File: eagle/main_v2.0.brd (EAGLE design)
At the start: 95 x 78 mm, 97 parts, among them IC1 74HC257D, IC2 PCA9530, IC3 RAC04, IC4 CS8416, IC5 MCP130-300I/SN, IC6 MAX1724, K1 G6A-234P, T1 BC847, T2 BC857, T3 BC847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

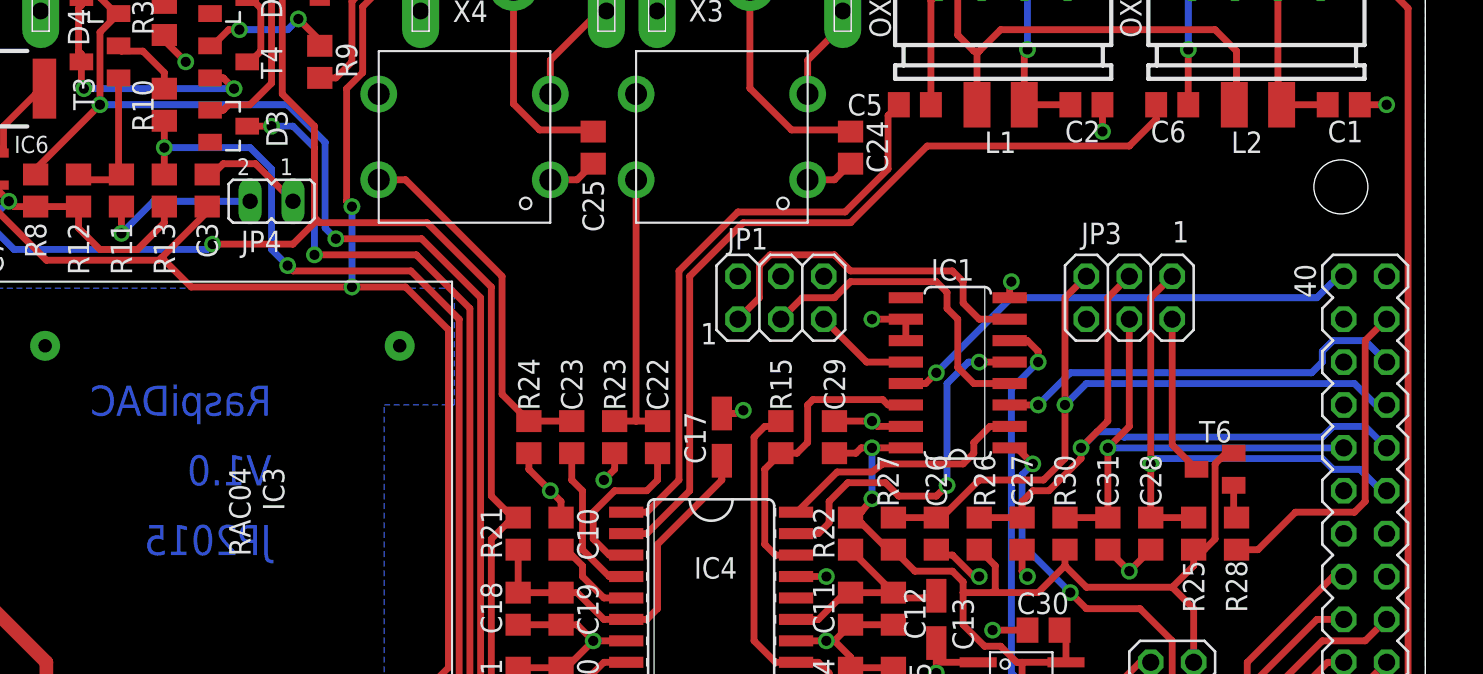
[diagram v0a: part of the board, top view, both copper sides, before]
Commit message: Eagle-Files: V2.0, zusätzlichen Ausgang für Relais eingebaut
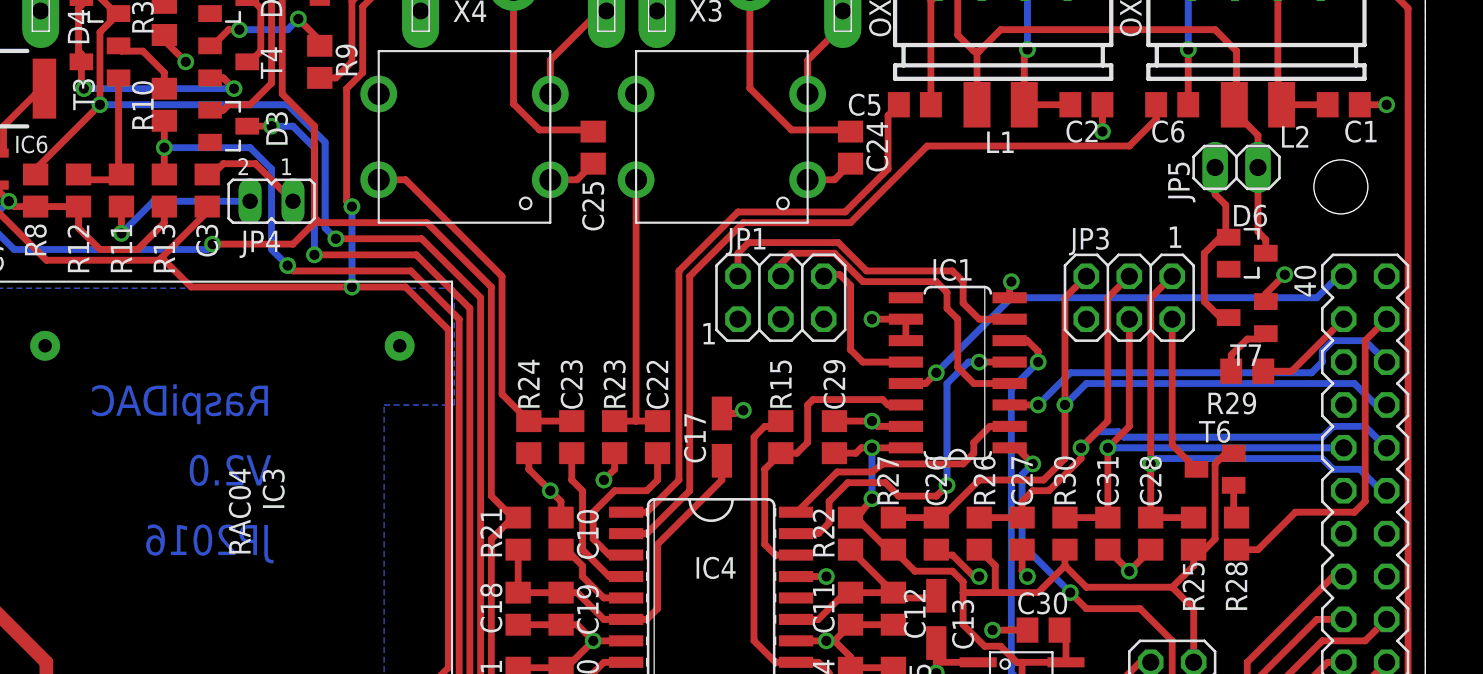
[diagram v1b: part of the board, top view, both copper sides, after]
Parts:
- added D6: BAS40, diode:SOT23
- added JP5: (no value), pinhead:1X02
- added R29: 10k, rcl:R0805
- added T7: BC847, transistor:SOT23-BEC
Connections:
- new net GPIO20: CON1.38, R29.1
- new net N$52: D6.1, JP5.1, T7.C
- new net N$55: R29.2, T7.B
- net +5V: now also D6.3, JP5.2
- net GND: now also JP1.1, JP1.3, JP1.5, T7.E; no longer JP1.2, JP1.4, JP1.6
- net N$26: now also JP1.2; no longer JP1.1
- net N$27: now also JP1.4; no longer JP1.3
- net N$53: now also JP1.6; no longer JP1.5
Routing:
- net N$52: track 0.00 -> 11.0 mm
- net +5V: track 268.1 -> 277.7 mm
- net GPIO20: track 0.00 -> 6.04 mm
- net N$55: track 0.00 -> 3.53 mm
- net N$53: track 5.92 -> 9.28 mm
- net GND: track 92.1 -> 94.5 mm, vias 27 -> 28
- net N$27: track 19.2 -> 20.0 mm
- net N$26: track 21.1 -> 20.3 mm
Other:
- board text added: "JP2016"
- board text added: "V2.0"
- board text removed: "JP2015"
- board text removed: "V1.0"
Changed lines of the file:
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@@
 <circle x="4" y="62" radius="2.75" width="0" layer="42"/>
 <text x="26.67" y="42.45" size="1.778" layer="16" font="vector" ratio="16" rot="MR0">RaspiDAC</text>
-<text x="26.67" y="38.3225" size="1.778" layer="16" font="vector" ratio="16" rot="MR0">V1.0</text>
-<text x="26.67" y="34.195" size="1.778" layer="16" font="vector" ratio="16" rot="MR0">JP2015</text>
+<text x="26.67" y="38.3225" size="1.778" layer="16" font="vector" ratio="16" rot="MR0">V2.0</text>
+<text x="26.67" y="34.195" size="1.778" layer="16" font="vector" ratio="16" rot="MR0">JP2016</text>
 <hole x="4" y="43" drill="3.2"/>
 <circle x="4" y="43" radius="2.75" width="0" layer="42"/>
-<text x="80.01" y="52.705" size="1.27" layer="21">1</text>
+<text x="79.6925" y="52.3875" size="1.27" layer="21">1</text>
 <text x="52.07" y="46.6725" size="1.27" layer="21">1</text>
 <text x="83.185" y="22.225" size="1.27" layer="21">1</text>
@@
 <elements>
 <element name="C1" library="rcl" package="C0805" value="100n" x="90.17" y="60.865" smashed="yes">
-<attribute name="NAME" x="89.2175" y="58.6425" size="1.27" layer="25"/>
+<attribute name="NAME" x="90.17" y="58.6425" size="1.27" layer="25"/>
 <attribute name="VALUE" x="88.9" y="58.325" size="1.27" layer="27"/>
 </element>
@@
 </element>
 <element name="JP3" library="pinhead" package="2X03" value="" x="77.47" y="49.435" smashed="yes" rot="R180">
-<attribute name="NAME" x="74.6125" y="52.61" size="1.27" layer="25" ratio="10"/>
+<attribute name="NAME" x="73.9775" y="52.2925" size="1.27" layer="25" ratio="10"/>
 <attribute name="VALUE" x="81.28" y="53.88" size="1.27" layer="27" rot="R180"/>
 </element>
@@
 </element>
 <element name="L2" library="user" package="C1210" value="47µ" x="85.09" y="60.865" smashed="yes">
-<attribute name="NAME" x="83.5025" y="58.0075" size="1.27" layer="25"/>
+<attribute name="NAME" x="86.36" y="58.325" size="1.27" layer="25"/>
 <attribute name="VALUE" x="83.185" y="57.69" size="1.27" layer="27"/>
 </element>
@@
 <attribute name="NAME" x="3.7475" y="65.92" size="1.27" layer="25"/>
 <attribute name="VALUE" x="3.69" y="75.31" size="1.27" layer="27" rot="R270"/>
+</element>
+<element name="D6" library="diode" package="SOT23" value="BAS40" x="84.455" y="52.07" smashed="yes" rot="R270">
+<attribute name="NAME" x="85.725" y="54.9275" size="1.27" layer="25" rot="R180"/>
+<attribute name="VALUE" x="81.28" y="53.975" size="1.27" layer="27" rot="R270"/>
+</element>
+<element name="T7" library="transistor" package="SOT23-BEC" value="BC847" x="84.455" y="48.26" smashed="yes" rot="R90">
+<attribute name="NAME" x="85.4075" y="46.6725" size="1.27" layer="25" rot="R180"/>
+<attribute name="VALUE" x="87.63" y="46.355" size="1.27" layer="27" rot="R90"/>
+</element>
+<element name="R29" library="rcl" package="R0805" value="10k" x="84.455" y="45.085" rot="R180"/>
+<element name="JP5" library="pinhead" package="1X02" value="" x="83.82" y="57.15" smashed="yes">
+<attribute name="NAME" x="81.0387" y="55.1688" size="1.27" layer="25" ratio="10" rot="R90"/>
+<attribute name="VALUE" x="81.28" y="53.975" size="1.27" layer="27"/>
 </element>
 </elements>
@@
 <contactref element="R3" pad="1"/>
 <contactref element="T1" pad="E"/>
-<contactref element="JP1" pad="2"/>
-<contactref element="JP1" pad="4"/>
-<contactref element="JP1" pad="6"/>
 <contactref element="T5" pad="E"/>
 <contactref element="CON1" pad="9"/>
@@
 <wire x1="57.785" y1="19.2725" x2="57.785" y2="20.1742" width="0.4064" layer="1"/>
 <wire x1="57.785" y1="20.1742" x2="57.7342" y2="20.225" width="0.4064" layer="1"/>
+<contactref element="JP1" pad="1"/>
+<contactref element="JP1" pad="3"/>
+<contactref element="JP1" pad="5"/>
+<contactref element="T7" pad="E"/>
+<wire x1="85.555" y1="49.21" x2="85.555" y2="49.6775" width="0.4064" layer="1"/>
+<wire x1="85.555" y1="49.6775" x2="86.6775" y2="50.8" width="0.4064" layer="1"/>
+<via x="86.6775" y="50.8" extent="1-16" drill="0.6"/>
+<wire x1="86.6775" y1="50.8" x2="86.36" y2="50.8" width="0.4064" layer="16"/>
 </signal>
 <signal name="+5V">
@@
 <wire x1="75.24350625" y1="12.2875" x2="74.769253125" y2="12.448246875" width="0.4064" layer="1"/>
 <wire x1="35.7825" y1="70.39" x2="32.0675" y2="66.675" width="0.4064" layer="1"/>
+<contactref element="D6" pad="3"/>
+<contactref element="JP5" pad="2"/>
+<wire x1="85.555" y1="52.07" x2="85.555" y2="52.875" width="0.4064" layer="1"/>
+<wire x1="85.555" y1="52.875" x2="85.09" y2="53.34" width="0.4064" layer="1"/>
+<wire x1="85.09" y1="53.34" x2="85.09" y2="57.15" width="0.4064" layer="1"/>
+<wire x1="83.69" y1="60.865" x2="83.69" y2="60.455" width="0.4064" layer="1"/>
+<wire x1="83.69" y1="60.455" x2="85.09" y2="59.055" width="0.4064" layer="1"/>
+<wire x1="85.09" y1="59.055" x2="85.09" y2="57.15" width="0.4064" layer="1"/>
 </signal>
 <signal name="+3V3">
@@
 <signal name="N$26">
 <contactref element="IC1" pad="7"/>
-<contactref element="JP1" pad="1"/>
 <wire x1="70.3834" y1="48.165" x2="68.58" y2="48.165" width="0.4064" layer="1"/>
 <wire x1="68.58" y1="48.165" x2="67.6275" y2="49.1175" width="0.4064" layer="1"/>
 <wire x1="67.6275" y1="49.1175" x2="67.6275" y2="50.3875" width="0.4064" layer="1"/>
 <wire x1="67.6275" y1="50.3875" x2="66.9925" y2="51.0225" width="0.4064" layer="1"/>
-<wire x1="66.9925" y1="51.0225" x2="60.96" y2="51.0225" width="0.4064" layer="1"/>
-<wire x1="60.96" y1="51.0225" x2="60.0075" y2="51.975" width="0.4064" layer="1"/>
-<wire x1="60.0075" y1="51.975" x2="56.1975" y2="51.975" width="0.4064" layer="1"/>
-<wire x1="56.1975" y1="51.975" x2="55.5625" y2="51.34" width="0.4064" layer="1"/>
-<wire x1="55.5625" y1="51.34" x2="55.5625" y2="49.435" width="0.4064" layer="1"/>
-<wire x1="55.5625" y1="49.435" x2="54.2925" y2="48.165" width="0.4064" layer="1"/>
+<wire x1="66.9925" y1="51.0225" x2="61.9125" y2="51.0225" width="0.4064" layer="1"/>
+<contactref element="JP1" pad="2"/>
+<wire x1="54.2925" y1="50.705" x2="54.2925" y2="52.07" width="0.4064" layer="1"/>
+<wire x1="54.2925" y1="52.07" x2="54.9275" y2="52.705" width="0.4064" layer="1"/>
+<wire x1="54.9275" y1="52.705" x2="60.23" y2="52.705" width="0.4064" layer="1"/>
+<wire x1="60.23" y1="52.705" x2="61.9125" y2="51.0225" width="0.4064" layer="1"/>
 </signal>
 <signal name="N$27">
-<contactref element="JP1" pad="3"/>
 <contactref element="IC1" pad="4"/>
 <wire x1="70.3834" y1="44.355" x2="68.2625" y2="44.355" width="0.4064" layer="1"/>
@@
 <wire x1="66.675" y1="48.8" x2="66.675" y2="49.7525" width="0.4064" layer="1"/>
 <wire x1="66.675" y1="49.7525" x2="66.04" y2="50.3875" width="0.4064" layer="1"/>
-<wire x1="66.04" y1="50.3875" x2="60.96" y2="50.3875" width="0.4064" layer="1"/>
-<wire x1="60.96" y1="50.3875" x2="60.0075" y2="49.435" width="0.4064" layer="1"/>
-<wire x1="60.0075" y1="49.435" x2="58.1025" y2="49.435" width="0.4064" layer="1"/>
-<wire x1="58.1025" y1="49.435" x2="56.8325" y2="48.165" width="0.4064" layer="1"/>
+<contactref element="JP1" pad="4"/>
+<wire x1="66.04" y1="50.3875" x2="61.69" y2="50.3875" width="0.4064" layer="1"/>
+<wire x1="61.69" y1="50.3875" x2="60.0075" y2="52.07" width="0.4064" layer="1"/>
+<wire x1="60.0075" y1="52.07" x2="57.4675" y2="52.07" width="0.4064" layer="1"/>
+<wire x1="57.4675" y1="52.07" x2="56.8325" y2="51.435" width="0.4064" layer="1"/>
+<wire x1="56.8325" y1="51.435" x2="56.8325" y2="50.705" width="0.4064" layer="1"/>
 </signal>
 <signal name="N$53">
 <contactref element="IC1" pad="12"/>
-<contactref element="JP1" pad="5"/>
-<wire x1="64.2366" y1="45.625" x2="61.9125" y2="45.625" width="0.4064" layer="1"/>
-<wire x1="61.9125" y1="45.625" x2="59.3725" y2="48.165" width="0.4064" layer="1"/>
+<wire x1="64.2366" y1="45.625" x2="61.69" y2="45.625" width="0.4064" layer="1"/>
+<contactref element="JP1" pad="6"/>
+<wire x1="61.69" y1="45.625" x2="60.96" y2="46.355" width="0.4064" layer="1"/>
+<wire x1="60.96" y1="46.355" x2="60.96" y2="50.165" width="0.4064" layer="1"/>
+<wire x1="60.96" y1="50.165" x2="60.325" y2="50.8" width="0.4064" layer="1"/>
+<wire x1="60.325" y1="50.8" x2="59.4675" y2="50.8" width="0.4064" layer="1"/>
+<wire x1="59.4675" y1="50.8" x2="59.3725" y2="50.705" width="0.4064" layer="1"/>
 </signal>
 <signal name="N$28">
@@
 <wire x1="13.335" y1="25.1625" x2="13.26" y2="25.0875" width="0.8128" layer="1"/>
 </signal>
+<signal name="N$52">
+<contactref element="T7" pad="C"/>
+<contactref element="D6" pad="1"/>
+<contactref element="JP5" pad="1"/>
+<wire x1="83.355" y1="48.26" x2="82.8675" y2="48.26" width="0.4064" layer="1"/>
+<wire x1="82.8675" y1="48.26" x2="81.915" y2="49.2125" width="0.4064" layer="1"/>
+<wire x1="81.915" y1="49.2125" x2="81.915" y2="52.07" width="0.4064" layer="1"/>
+<wire x1="81.915" y1="52.07" x2="82.8675" y2="53.0225" width="0.4064" layer="1"/>
+<wire x1="82.8675" y1="53.0225" x2="83.3525" y2="53.0225" width="0.4064" layer="1"/>
+<wire x1="83.3525" y1="53.0225" x2="83.355" y2="53.02" width="0.4064" layer="1"/>
+<wire x1="82.55" y1="57.15" x2="82.55" y2="55.5625" width="0.4064" layer="1"/>
+<wire x1="82.55" y1="55.5625" x2="83.185" y2="54.9275" width="0.4064" layer="1"/>
+<wire x1="83.185" y1="54.9275" x2="83.185" y2="53.19" width="0.4064" layer="1"/>
+<wire x1="83.185" y1="53.19" x2="83.355" y2="53.02" width="0.4064" layer="1"/>
+</signal>
+<signal name="N$55">
+<contactref element="T7" pad="B"/>
+<contactref element="R29" pad="2"/>
+<wire x1="83.505" y1="45.085" x2="83.505" y2="46.04" width="0.4064" layer="1"/>
+<wire x1="83.505" y1="46.04" x2="84.455" y2="46.99" width="0.4064" layer="1"/>
+<wire x1="84.455" y1="46.99" x2="85.235" y2="46.99" width="0.4064" layer="1"/>
+<wire x1="85.235" y1="46.99" x2="85.555" y2="47.31" width="0.4064" layer="1"/>
+</signal>
+<signal name="GPIO20">
+<contactref element="CON1" pad="38"/>
+<contactref element="R29" pad="1"/>
+<wire x1="85.405" y1="45.085" x2="87.09" y2="45.085" width="0.4064" layer="1"/>
+<wire x1="87.09" y1="45.085" x2="90.17" y2="48.165" width="0.4064" layer="1"/>
+</signal>
 </signals>

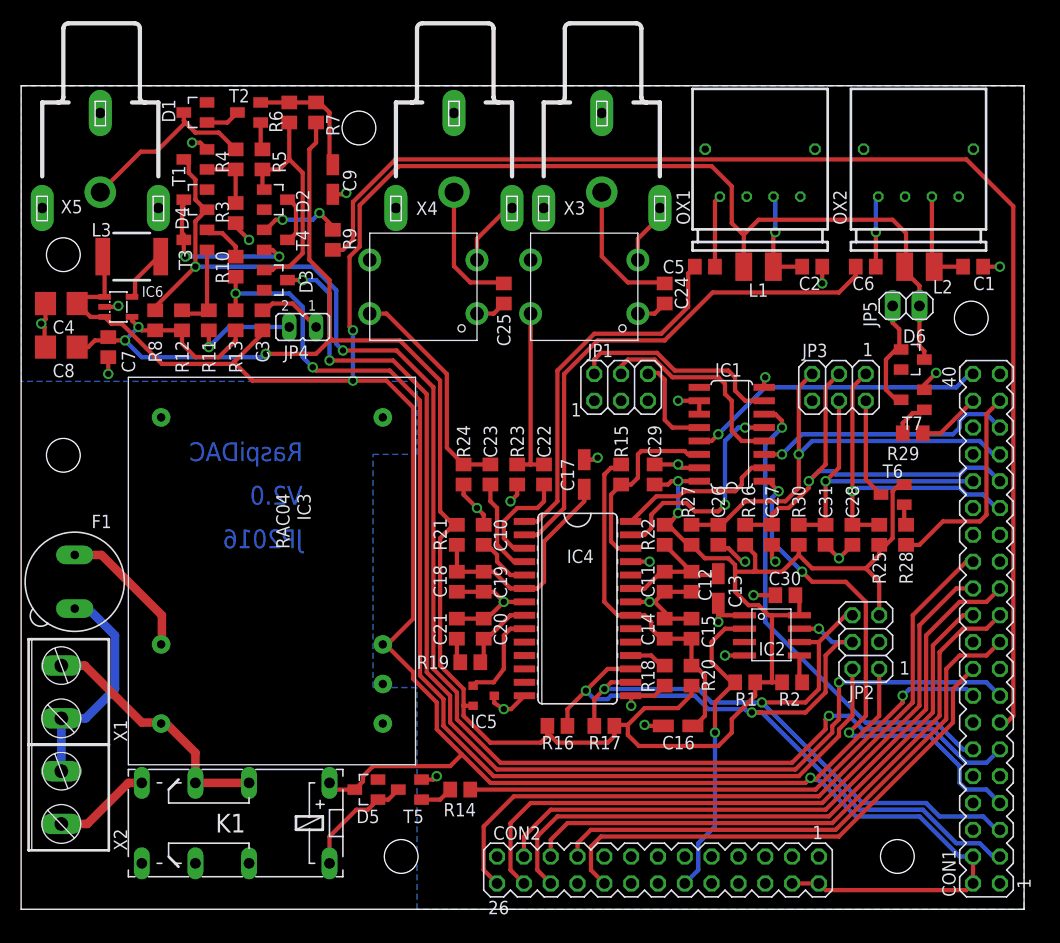
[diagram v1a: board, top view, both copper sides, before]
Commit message: Eagle V2.0: 3.3V Step-Down-Wandler ersetzt und Fehler behoben. Keine weiteren Anpassungen mehr nötig.
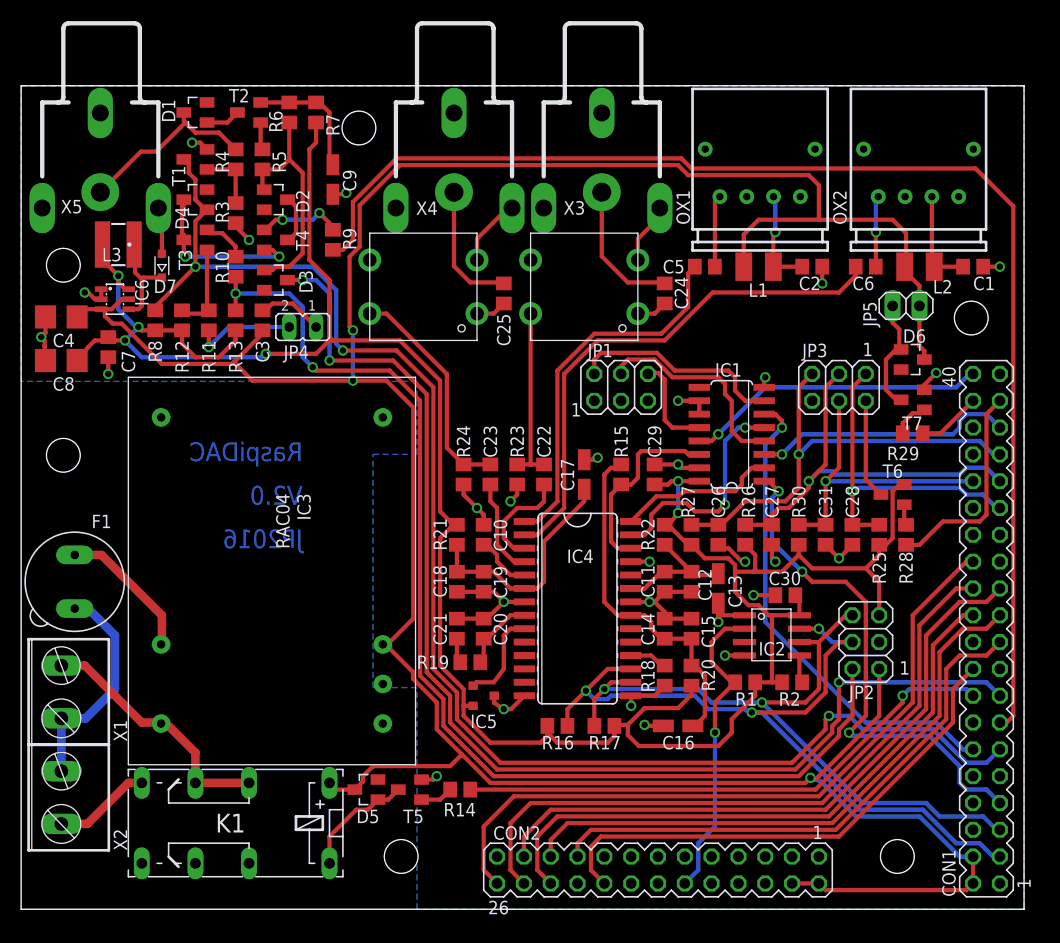
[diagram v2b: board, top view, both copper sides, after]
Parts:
- added D7: BAT165, dp_devices:SOD-323F
- IC6: value MAX1724 -> MAX1836; device MAX1724:SOT23-5L -> maxim-5:SOT23-6L
- L3: device inductor-coilcraft:DS1608 -> inductor-coilcraft:LPS4018
- moved L3 1.71 mm to (9.21, 63.0), turned to 180 degrees
- moved C4 1.27 mm to (3.81, 56.1)
- moved C8 1.27 mm to (3.81, 52.0)
- moved IC6 0.80 mm to (8.89, 57.8)
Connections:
- net +3V3: now also IC6.6, L3.2; no longer IC6.4
- net +5V: now also IC6.5; no longer IC6.1, L3.1
- net GND: now also D7.A, IC6.1
- net N$28: now also D7.C, IC6.4, L3.1; no longer IC6.5, L3.2
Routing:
- net +3V3: track 226.2 -> 237.5 mm, vias 5 -> 6
- net GND: track 94.5 -> 100.4 mm
- net N$28: track 5.01 -> 9.44 mm
- net +5V: track 277.7 -> 281.2 mm
